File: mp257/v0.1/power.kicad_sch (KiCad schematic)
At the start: 135 parts, among them U1 STM32MP257FAK3, U26 STPMIC25APQR, U9 MCP1501-18xCH

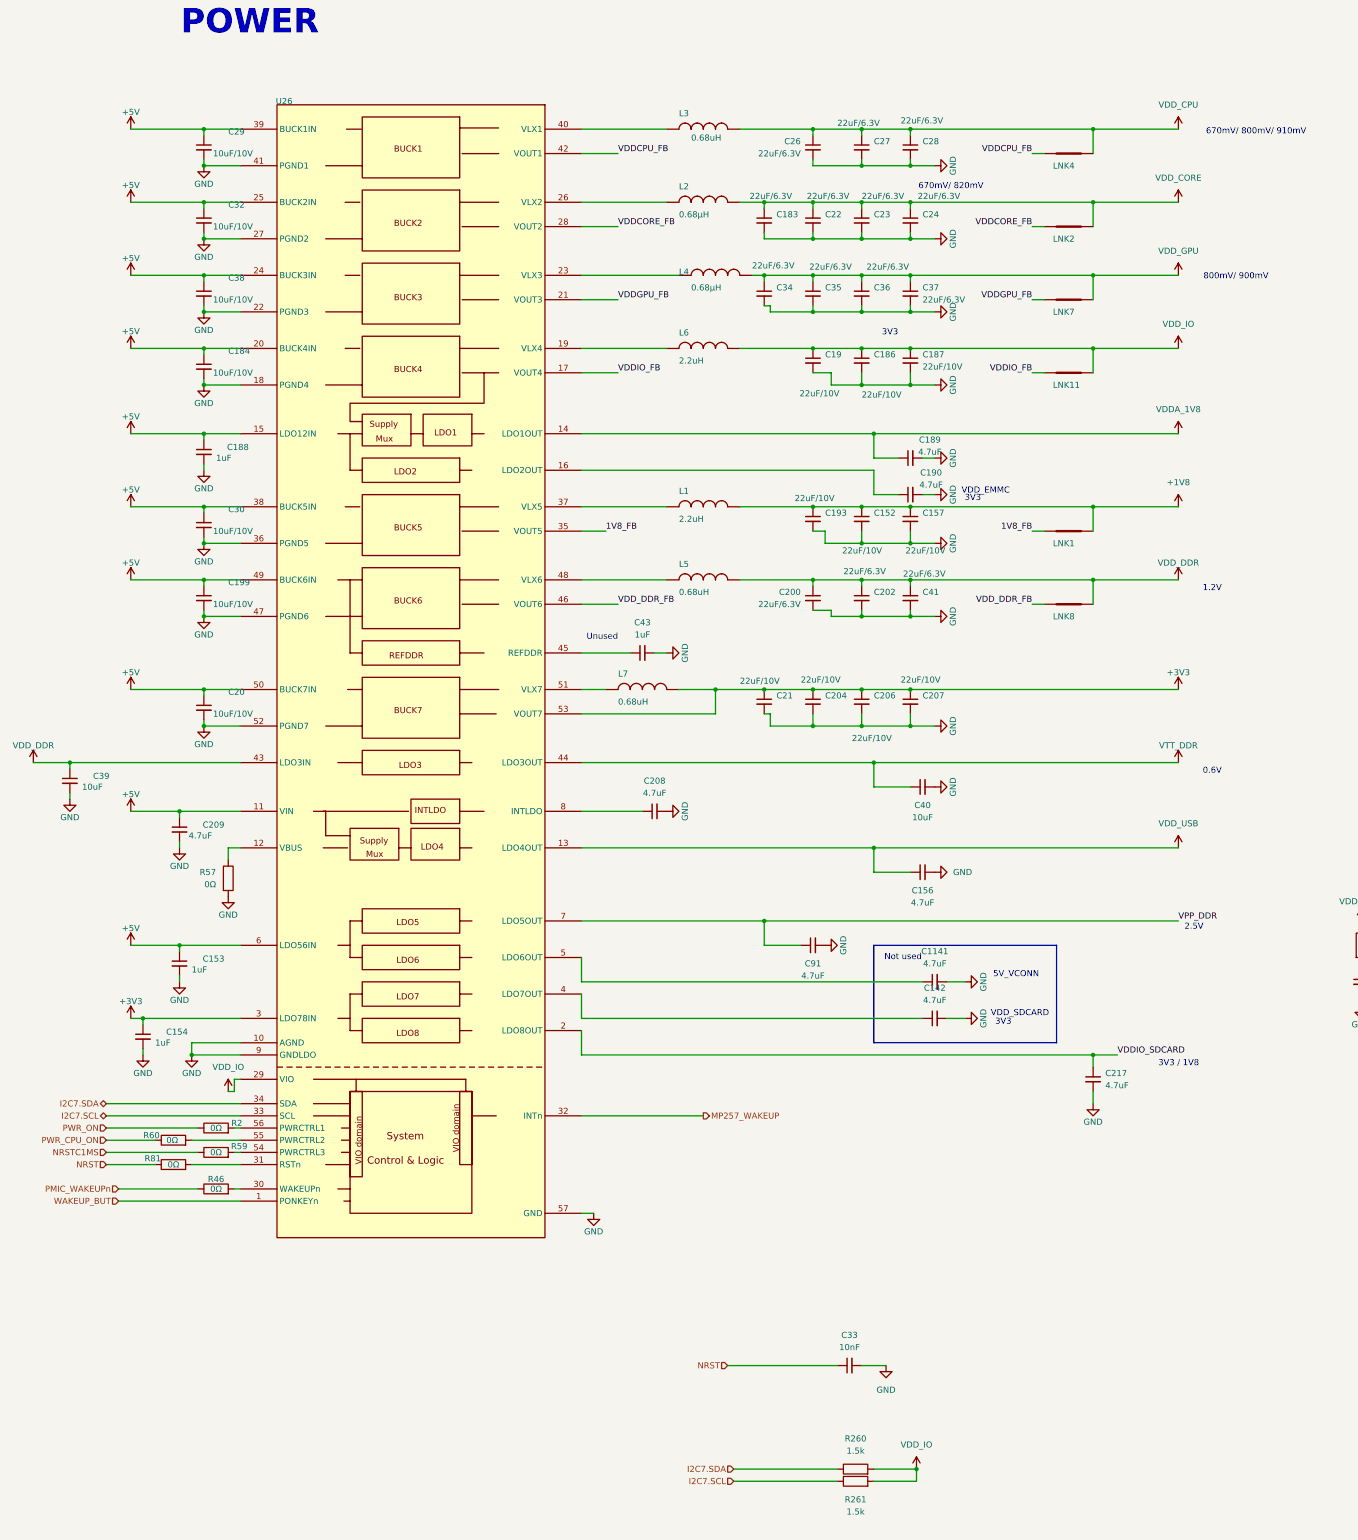
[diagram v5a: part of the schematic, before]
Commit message: Update remaining parts to 4ms lib
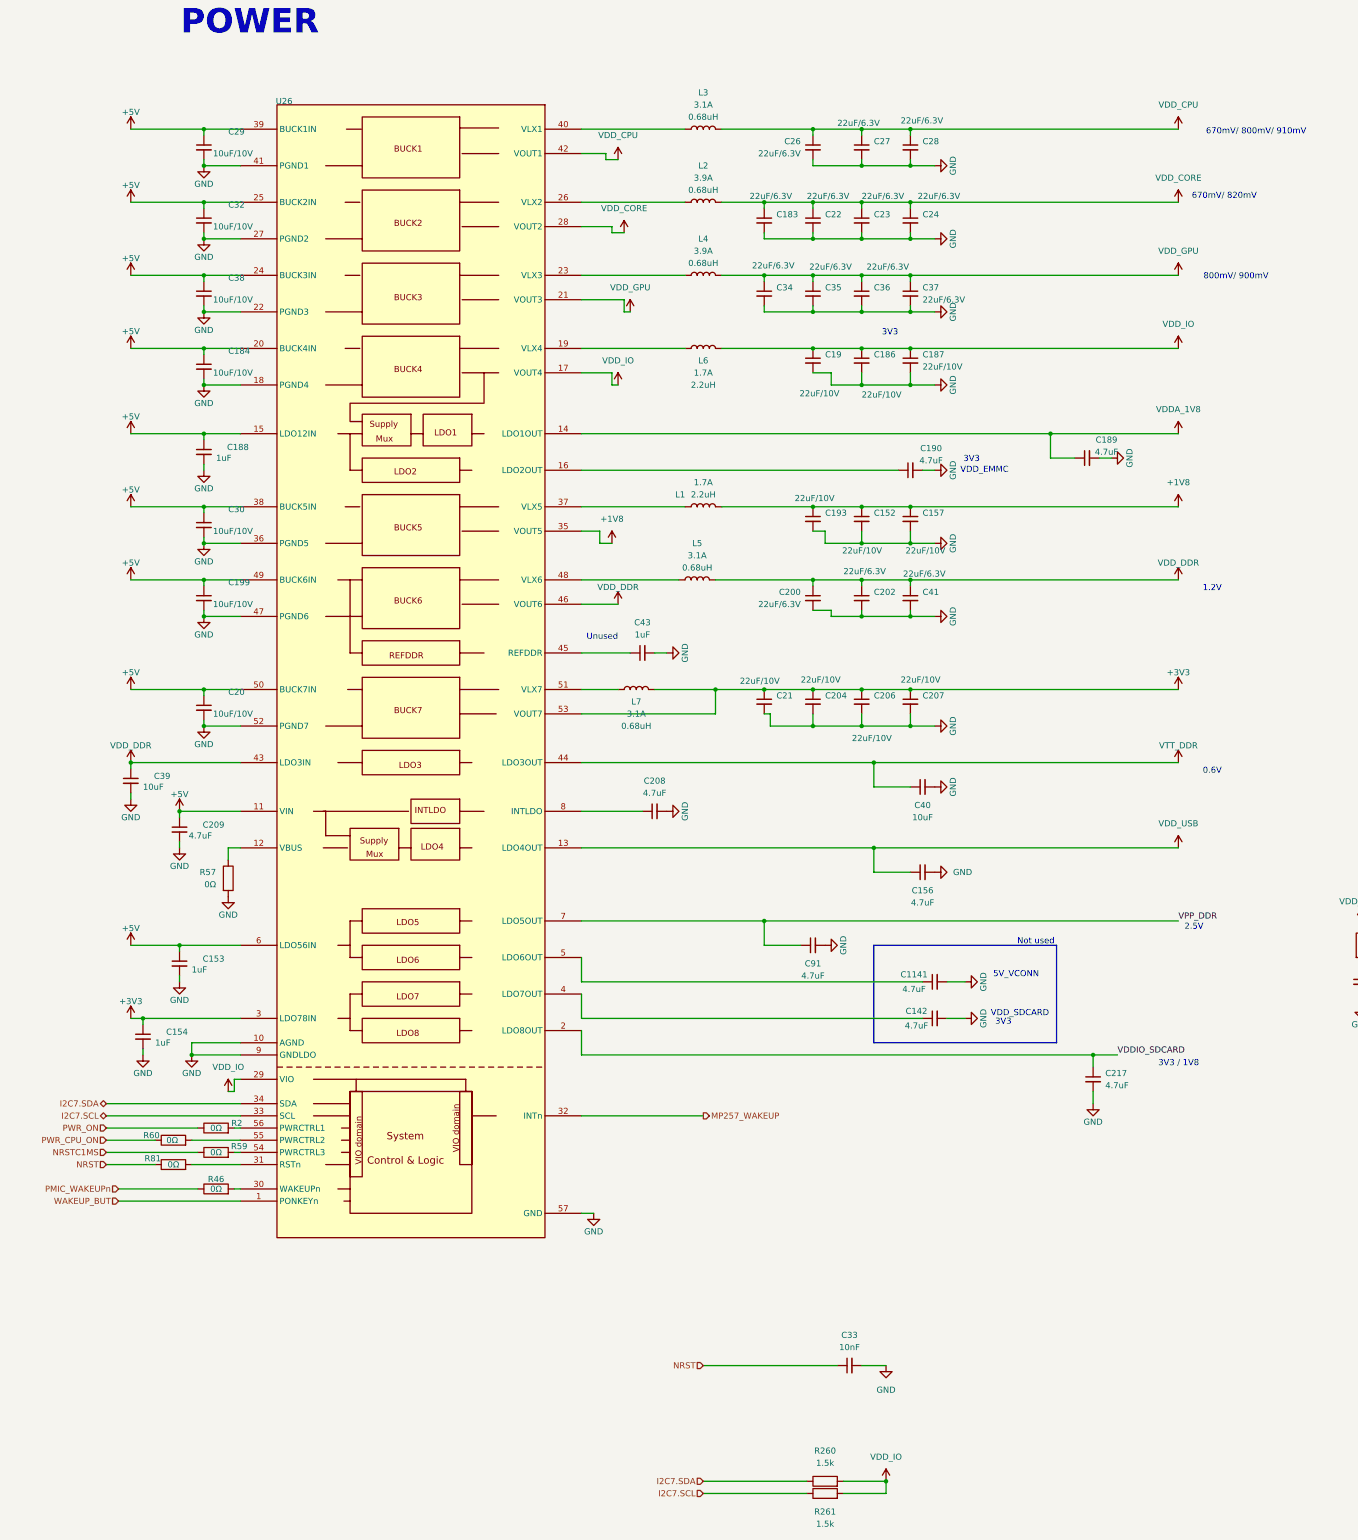
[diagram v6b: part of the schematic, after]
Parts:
- removed LNK1, LNK11, LNK2, LNK7, LNK8: ${ALTIUM_VALUE}, LINK200, symbol MCD_PARTS_database:U_PMIC_3_link_200_MCD_PARTS_database.DbLib
- removed LNK4: ${ALTIUM_VALUE}, LINK200, symbol MCD_PARTS_database:U_PMIC_1_link_200_MCD_PARTS_database.DbLib
- L1, L6: value Inductor -> 2.2uH_1.7A_2016; footprint IND_2016_MURATA_LQM2MPN2R2NG0 -> 4ms_Inductor:COIL_2016_Murata_Handsolder; symbol MCD_PARTS_database:U_PMIC_0_Inductor_MCD_PARTS_database.DbLib -> 4ms_Inductor:2.2uH_1.7A_2016; ALTIUM_VALUE 2.2uH -> (none); COMPONENTLINK1URL http://tunmcdsvn.tun.st.com/Component_Documentation_Library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 -> (none); COMPONENT_COUNTRY_OF_ORIGIN Vietnam -> (none); Display (none) -> 2.2uH; Display 2 (none) -> 1.7A; ID 5259 -> (none); INTERNAL_PART_NUMBER MCD-03143 -> (none); MANUFACTURER MURATA -> (none); MANUFACTURER_PART_NUMBER DFE201610E-2R2M=P2 -> (none); Manufacturer (none) -> Murata; ORDER_CODE_DIGIKEY 490-17728-2-ND - -> (none); ORDER_CODE_FARNELL N/A -> (none); ORDER_CODE_RS N/A -> (none); PACKAGE 0806 -> (none); PART_PREFERENCE Recommended -> (none); PART_TYPE Inductor -> (none); Part Number (none) -> DFE201610E-2R2M=P2; Production Stage (none) -> A; SHOWFIELDS YES -> (none); STATUS Checked -> (none); Specifications (none) -> 2.2uH, Isat>2.4A, Imax>=1.7A, Rdc<=120mOhms, shielded
- L2, L4: value Inductor -> 0.68uH_3.9A_2520; footprint IND_2520_TOKO_DFE252012P -> 4ms_Inductor:COIL_2520_Murata_Handsolder; symbol MCD_PARTS_database:U_PMIC_0_Inductor_MCD_PARTS_database.DbLib -> 4ms_Inductor:0.68uH_3.9A_2520; ALTIUM_VALUE 0.68µH -> (none); COMPONENTLINK1URL http://tunmcdsvn.tun.st.com/Component_Documentation_Library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 -> (none); COMPONENT_COUNTRY_OF_ORIGIN Vietnam -> (none); Display (none) -> 0.68uH; Display 2 (none) -> 3.9A; ID 5258 -> (none); INTERNAL_PART_NUMBER MCD-03142 -> (none); MANUFACTURER MURATA -> (none); MANUFACTURER_PART_NUMBER DFE252012F-R68M=P2 -> (none); Manufacturer (none) -> Murata; ORDER_CODE_DIGIKEY 490-13044-2-ND -> (none); ORDER_CODE_FARNELL N/A -> (none); ORDER_CODE_RS N/A -> (none); PACKAGE 1008 -> (none); PART_PREFERENCE Recommended -> (none); PART_TYPE Inductor -> (none); Part Number (none) -> DFE252012F-R68M=P2; Production Stage (none) -> A; SHOWFIELDS YES -> (none); STATUS Checked -> (none); Specifications (none) -> 0.68uH, Isat>5.4A, Imax>=3.9A, Rdc<=50mOhms, shielded
- L3, L5, L7: value Inductor -> 0.68uH_3.1A_2016; footprint IND_2016_MURATA_LQM2MPN2R2NG0 -> 4ms_Inductor:COIL_2016_Murata_Handsolder; symbol MCD_PARTS_database:U_PMIC_0_Inductor_MCD_PARTS_database.DbLib -> 4ms_Inductor:0.68uH_3.1A_2016; ALTIUM_VALUE 0.68uH -> (none); COMPONENTLINK1URL http://tunmcdsvn.tun.st.com/Component_Documentation_Library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 -> (none); COMPONENT_COUNTRY_OF_ORIGIN Vietnam -> (none); Display (none) -> 0.68uH; Display 2 (none) -> 3.1A; ID 5257 -> (none); INTERNAL_PART_NUMBER MCD-03141 -> (none); MANUFACTURER MURATA -> (none); MANUFACTURER_PART_NUMBER DFE201610E-R68M=P2 -> (none); Manufacturer (none) -> Murata; ORDER_CODE_DIGIKEY N/A -> (none); ORDER_CODE_FARNELL N/A -> (none); ORDER_CODE_RS N/A -> (none); PACKAGE 0806 -> (none); PART_PREFERENCE Recommended -> (none); PART_TYPE Inductor -> (none); Part Number (none) -> DFE201610E-R68M=P2; Production Stage (none) -> A; SHOWFIELDS YES -> (none); STATUS Checked -> (none); Specifications (none) -> 0.68uH, Isat>4.3A, Imax>=3.1A, Rdc<=50mOhms, shielded
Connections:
- net 1V8_FB is gone; now on net +1V8: U26.35 (VOUT5)
- net VDDCORE_FB is gone; now on net VDD_CORE: U26.28 (VOUT2)
- net VDDCPU_FB is gone; now on net VDD_CPU: U26.42 (VOUT1)
- net VDDGPU_FB is gone; now on net VDD_GPU: U26.21 (VOUT3)
- net VDDIO_FB is gone; now on net VDD_IO: U26.17 (VOUT4)
- net VDD_DDR_FB is gone; now on net VDD_DDR: U26.46 (VOUT6)
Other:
- moved on the sheet: C189, C190, C39, R260, R261

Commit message: WIP
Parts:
- C29: footprint 4ms_Capacitor:C_0603 -> C30
- C42: value 2.2uF_0603_25V -> 1uF_0402_25V; footprint 4ms_Capacitor:C_0603 -> 4ms_Capacitor:C_0402; symbol 4ms_Capacitor:2.2uF_0603_25V -> 4ms_Capacitor:1uF_0402_25V; Display 2.2uF -> 1uF; JLCPCB ID C57895 -> C52923; Manufacturer Murata -> Taiyo Yuden; Manufacturer 2 (none) -> Murata; Part Number GRM188R6YA225KA12D -> GMK105CC6105KV-F; Part Number 2 (none) -> GRM155C81E105ME11J; Specifications 2.2uF, Min 25V 10% X5R -> 1uF, Min. 25V, 0402, Ceramic/MLCC
- C53: value 10uF_0603_10V -> 10uF_0402_6.3V; footprint 4ms_Capacitor:C_0603 -> 4ms_Capacitor:C_0402; symbol 4ms_Capacitor:10uF_0603_10V -> 4ms_Capacitor:10uF_0402_6.3V; Display 10uF/10V -> 10uF; JLCPCB ID C19702 -> (none); Manufacturer Murata -> (none); Part Number GRM188R61A106KE69D -> (none); Specifications 10uF, Min. 10V X5R 10% -> 10uF, Min. 6.3V, 0402, Ceramic/MLCC
- L2, L4: footprint 4ms_Inductor:COIL_2520_Murata_Handsolder -> 4ms_Inductor:COIL_2520_TOKO_Handsolder
- renumbered NT1 to NT2
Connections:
- net +5V: now also C29.2, C30.2, C32.2, C38.2; no longer C29.1, C30.1, C32.1, C38.1
- net GND: now also C26.1, C27.1, C28.1, C29.1, C30.1, C32.1, C34.1, C35.1, C36.1, C37.1, C38.1, C39.1, C40.1, C41.1, C45.1, C46.1, C48.1, C49.1, C50.1; no longer C26.2, C27.2, C28.2, C29.2, C30.2, C32.2, C34.2, C35.2, C36.2, C37.2, C38.2, C39.2, C40.2, C41.2, C45.2, C46.2, C48.2, C49.2, C50.2
- net VDD_CORE: now also C45.2, C46.2, C48.2, C49.2, C50.2; no longer C45.1, C46.1, C48.1, C49.1, C50.1
- net VDD_CPU: now also C26.2, C27.2, C28.2; no longer C26.1, C27.1, C28.1
- net VDD_DDR: now also C39.2, C41.2; no longer C39.1, C41.1
- net VDD_GPU: now also C34.2, C35.2, C36.2, C37.2; no longer C34.1, C35.1, C36.1, C37.1
- net VTT_DDR: now also C40.2; no longer C40.1
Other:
- moved on the sheet: C26, C27, C28, C29, C30, C32, C34, C35, C36, C37, C38, C39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

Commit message: Fix caps
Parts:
- C29: footprint C30 -> 4ms_Capacitor:C_0603
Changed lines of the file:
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@@
 			)
 		)
-		(property "Footprint" "C30"
+		(property "Footprint" "4ms_Capacitor:C_0603"
 			(at 67.31 78.74 0)
 			(effects
